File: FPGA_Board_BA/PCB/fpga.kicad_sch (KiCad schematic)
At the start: 5 parts, among them J9 Box_Header_26pin, U2 Zynq7020

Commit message: some minimal changes on the PCB on the right side
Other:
- moved on the sheet: U2B, U2C, U2D

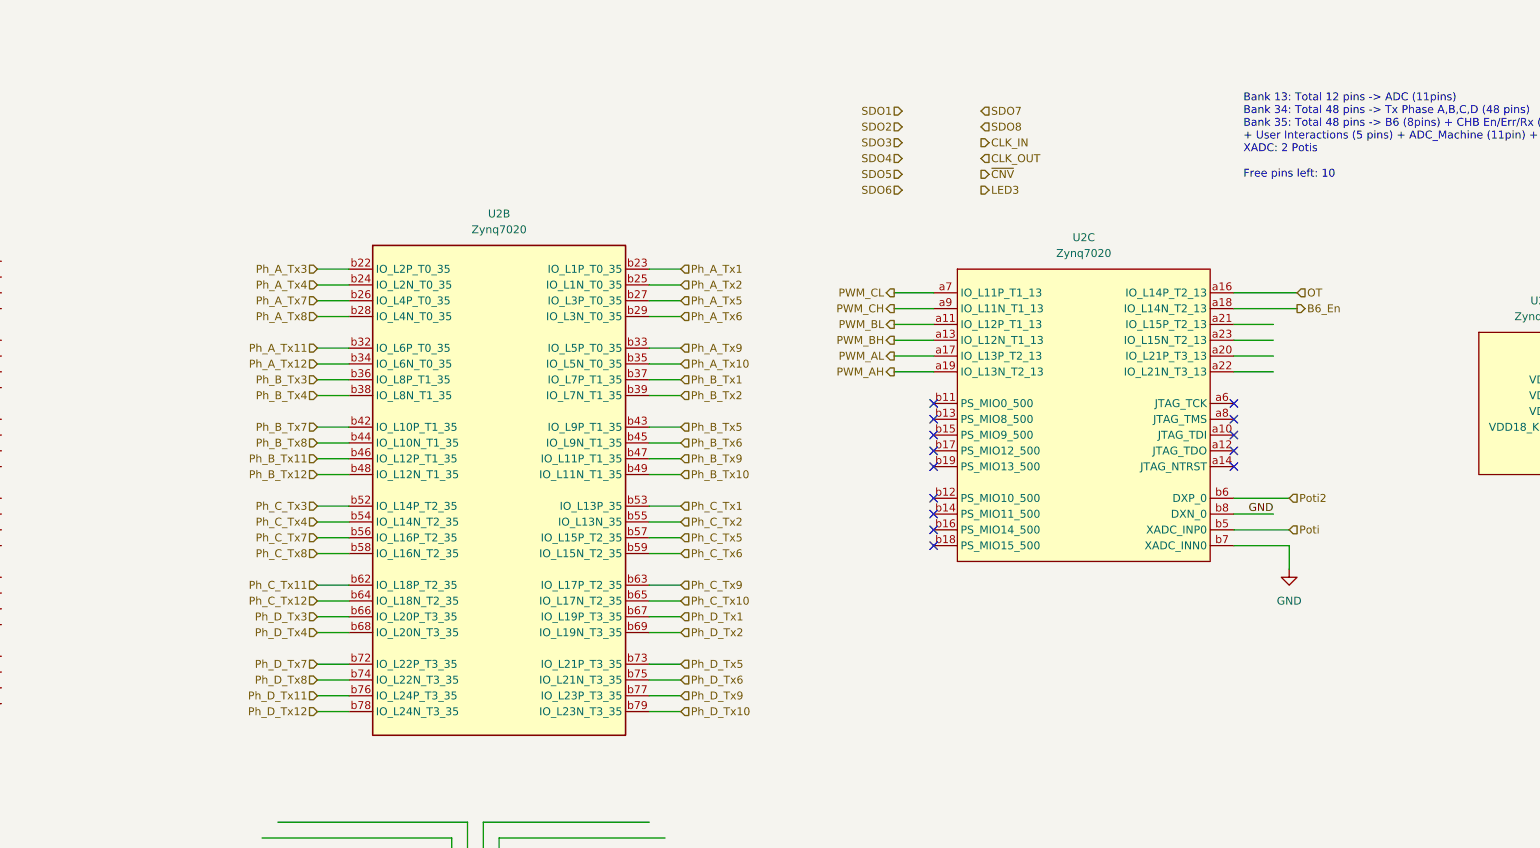
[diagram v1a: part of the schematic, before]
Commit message: added bus into schematic
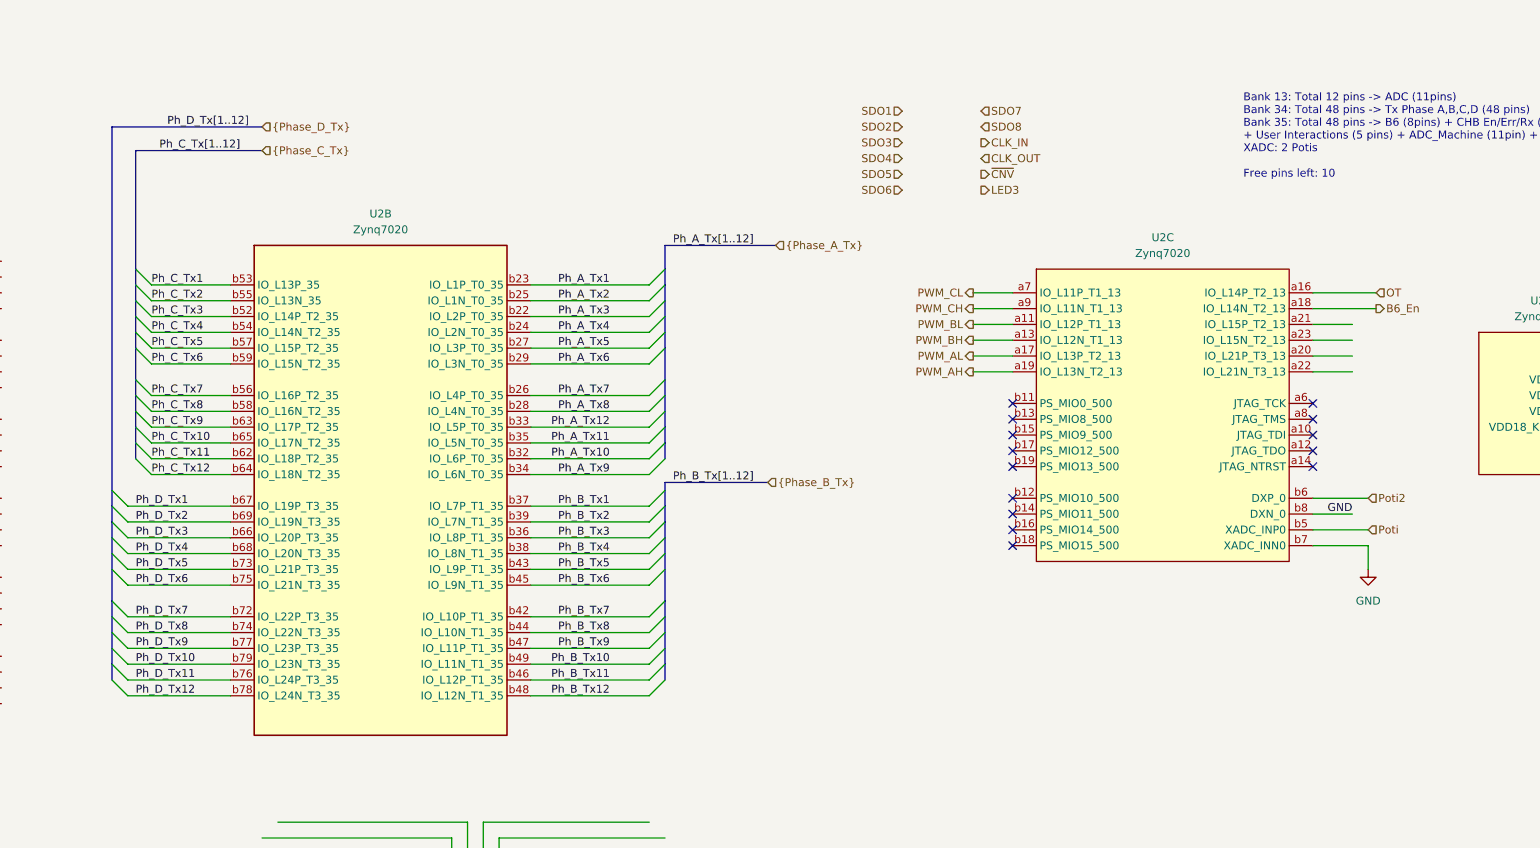
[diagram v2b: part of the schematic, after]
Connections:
- net Ph_A_Tx10: now also U2.b32 (IO_L6P_T0_35); no longer U2.b35 (IO_L5N_T0_35)
- net Ph_A_Tx11: now also U2.b35 (IO_L5N_T0_35); no longer U2.b32 (IO_L6P_T0_35)
- net Ph_A_Tx12: now also U2.b33 (IO_L5P_T0_35); no longer U2.b34 (IO_L6N_T0_35)
- net Ph_A_Tx9: now also U2.b34 (IO_L6N_T0_35); no longer U2.b33 (IO_L5P_T0_35)
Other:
- moved on the sheet: U2B, U2C

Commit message: big schematic cleanup. Added wire to bus
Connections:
- net B6_En: now also U2.a16 (IO_L14P_T2_13); no longer U2.a18 (IO_L14N_T2_13)
- net CLK_IN: now also U2.a38 (IO_L5N_T0_34)
- net CLK_OUT: now also U2.a36 (IO_L5P_T0_34)
- net OT: now also U2.a18 (IO_L14N_T2_13); no longer U2.a16 (IO_L14P_T2_13)
- net PWM_AH: now also U2.a7 (IO_L11P_T1_13); no longer U2.a19 (IO_L13N_T2_13)
- net PWM_AL: now also U2.a9 (IO_L11N_T1_13); no longer U2.a17 (IO_L13P_T2_13)
- net PWM_BH: now also U2.a11 (IO_L12P_T1_13); no longer U2.a13 (IO_L12N_T1_13)
- net PWM_BL: now also U2.a13 (IO_L12N_T1_13); no longer U2.a11 (IO_L12P_T1_13)
- net PWM_CH: now also U2.a17 (IO_L13P_T2_13); no longer U2.a9 (IO_L11N_T1_13)
- net PWM_CL: now also U2.a19 (IO_L13N_T2_13); no longer U2.a7 (IO_L11P_T1_13)
- net SDO1: now also U2.a26 (IO_L1P_T0_34)
- net SDO2: now also U2.a28 (IO_L1N_T0_34)
- net SDO3: now also U2.a27 (IO_L2P_T0_34)
- net SDO4: now also U2.a29 (IO_L2N_T0_34)
- net SDO5: now also U2.a30 (IO_L3P_T0_34)
- net SDO6: now also U2.a32 (IO_L3N_T0_34)
- net SDO7: now also U2.a31 (IO_L4P_T0_34)
- net SDO8: now also U2.a33 (IO_L4N_T0_34)
- net ~{CNV}: now also U2.a37 (IO_L6P_T0_34)
- net Err_Ph1: now reaches U2.a64 (IO_L19P_T3_34)
- net Err_Ph2: now reaches U2.a66 (IO_L19N_T3_34)
- net Err_Ph4: now reaches U2.a71 (IO_L20P_T3_34)
- net Err_Ph3: now reaches U2.a72 (IO_L20N_T3_34)
- net Rx_Ph2: now reaches U2.a73 (IO_L21N_T3_34)
- net Rx_Ph1: now reaches U2.a74 (IO_L21P_T3_34)
- net Rx_Ph3: now reaches U2.a75 (IO_L22P_T3_34)
- net En_Ph3: now reaches U2.a76 (IO_L24P_T3_34)
- net Rx_Ph4: now reaches U2.a77 (IO_L22N_T3_34)
- net En_Ph4: now reaches U2.a78 (IO_L24N_T3_34)
- net En_Ph1: now reaches U2.a79 (IO_L23P_T3_34)
- net En_Ph2: now reaches U2.a80 (IO_L23N_T3_34)
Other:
- moved on the sheet: U2A, U2B, U2C

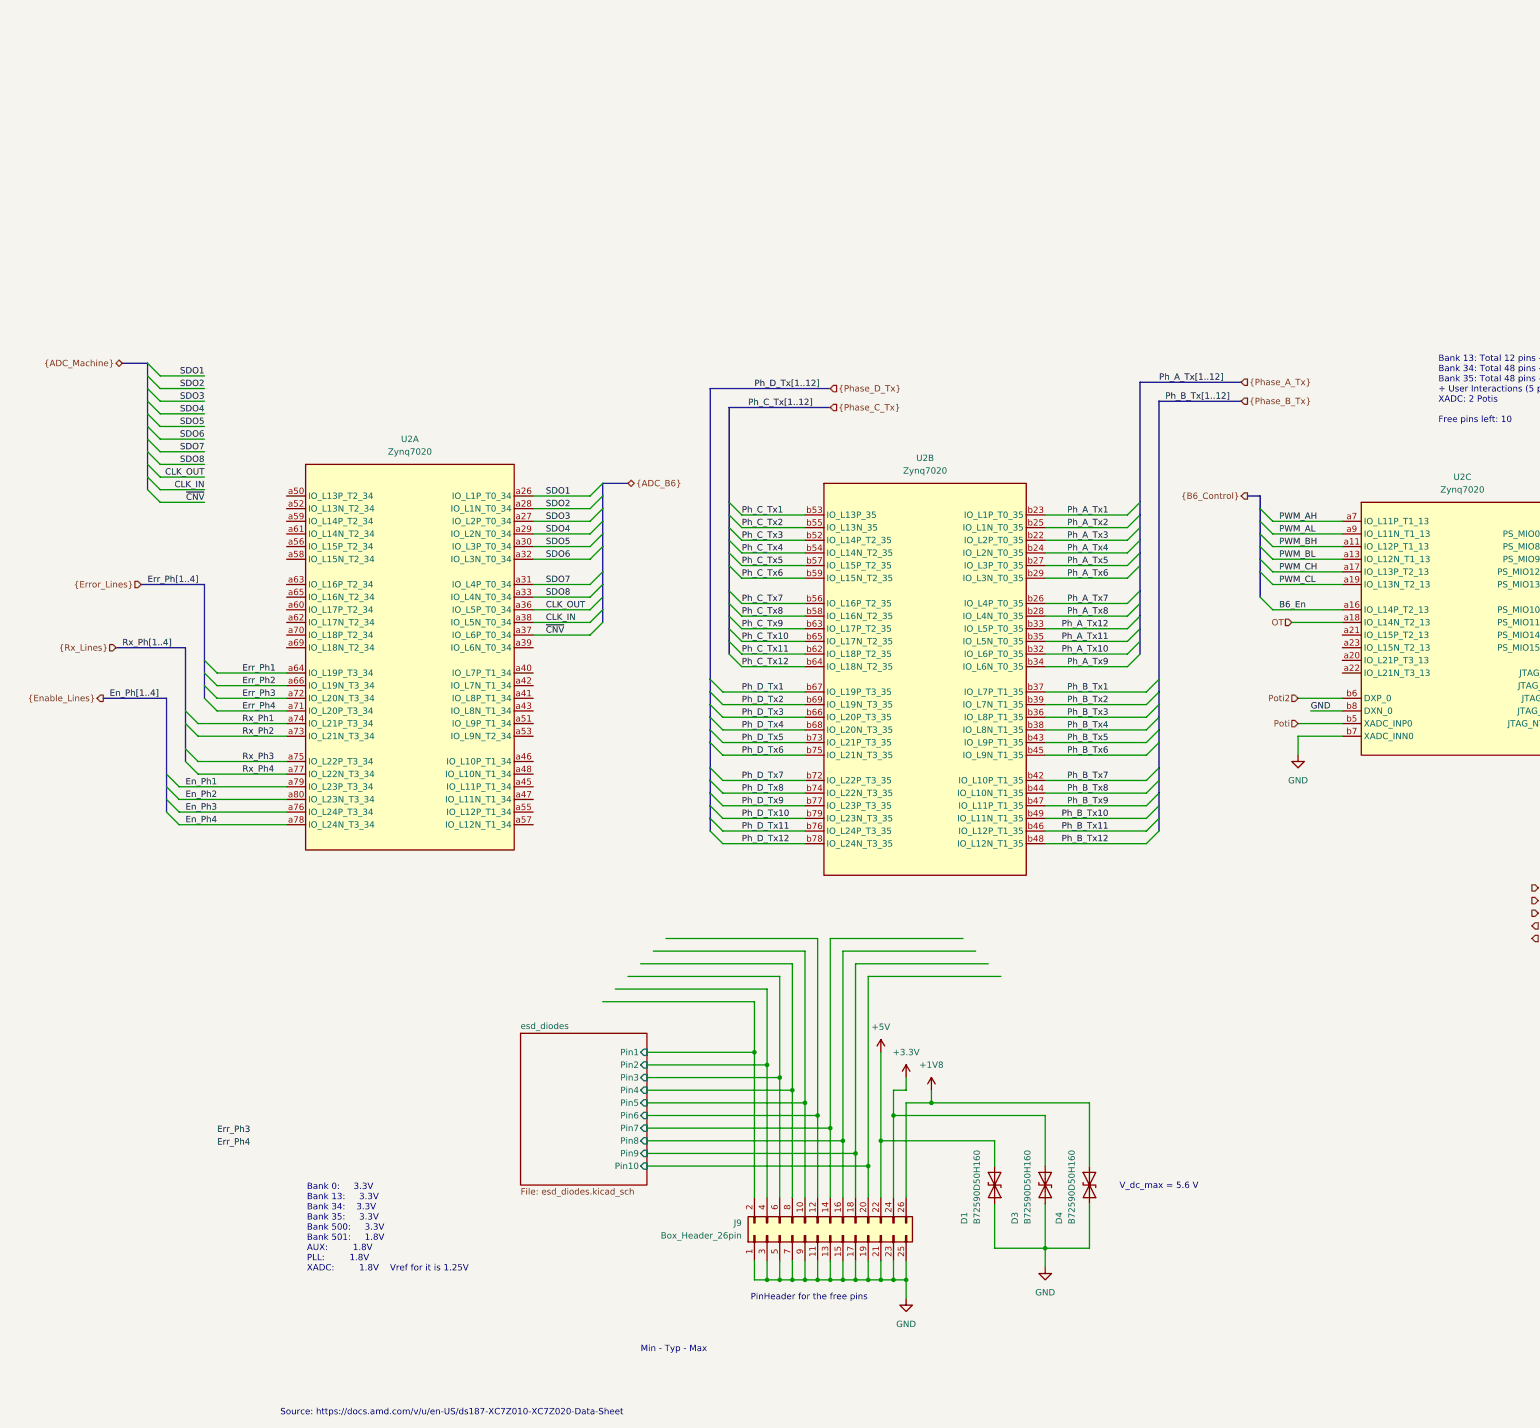
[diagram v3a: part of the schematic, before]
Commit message: PCB left side almost finished + some optimization in schematics
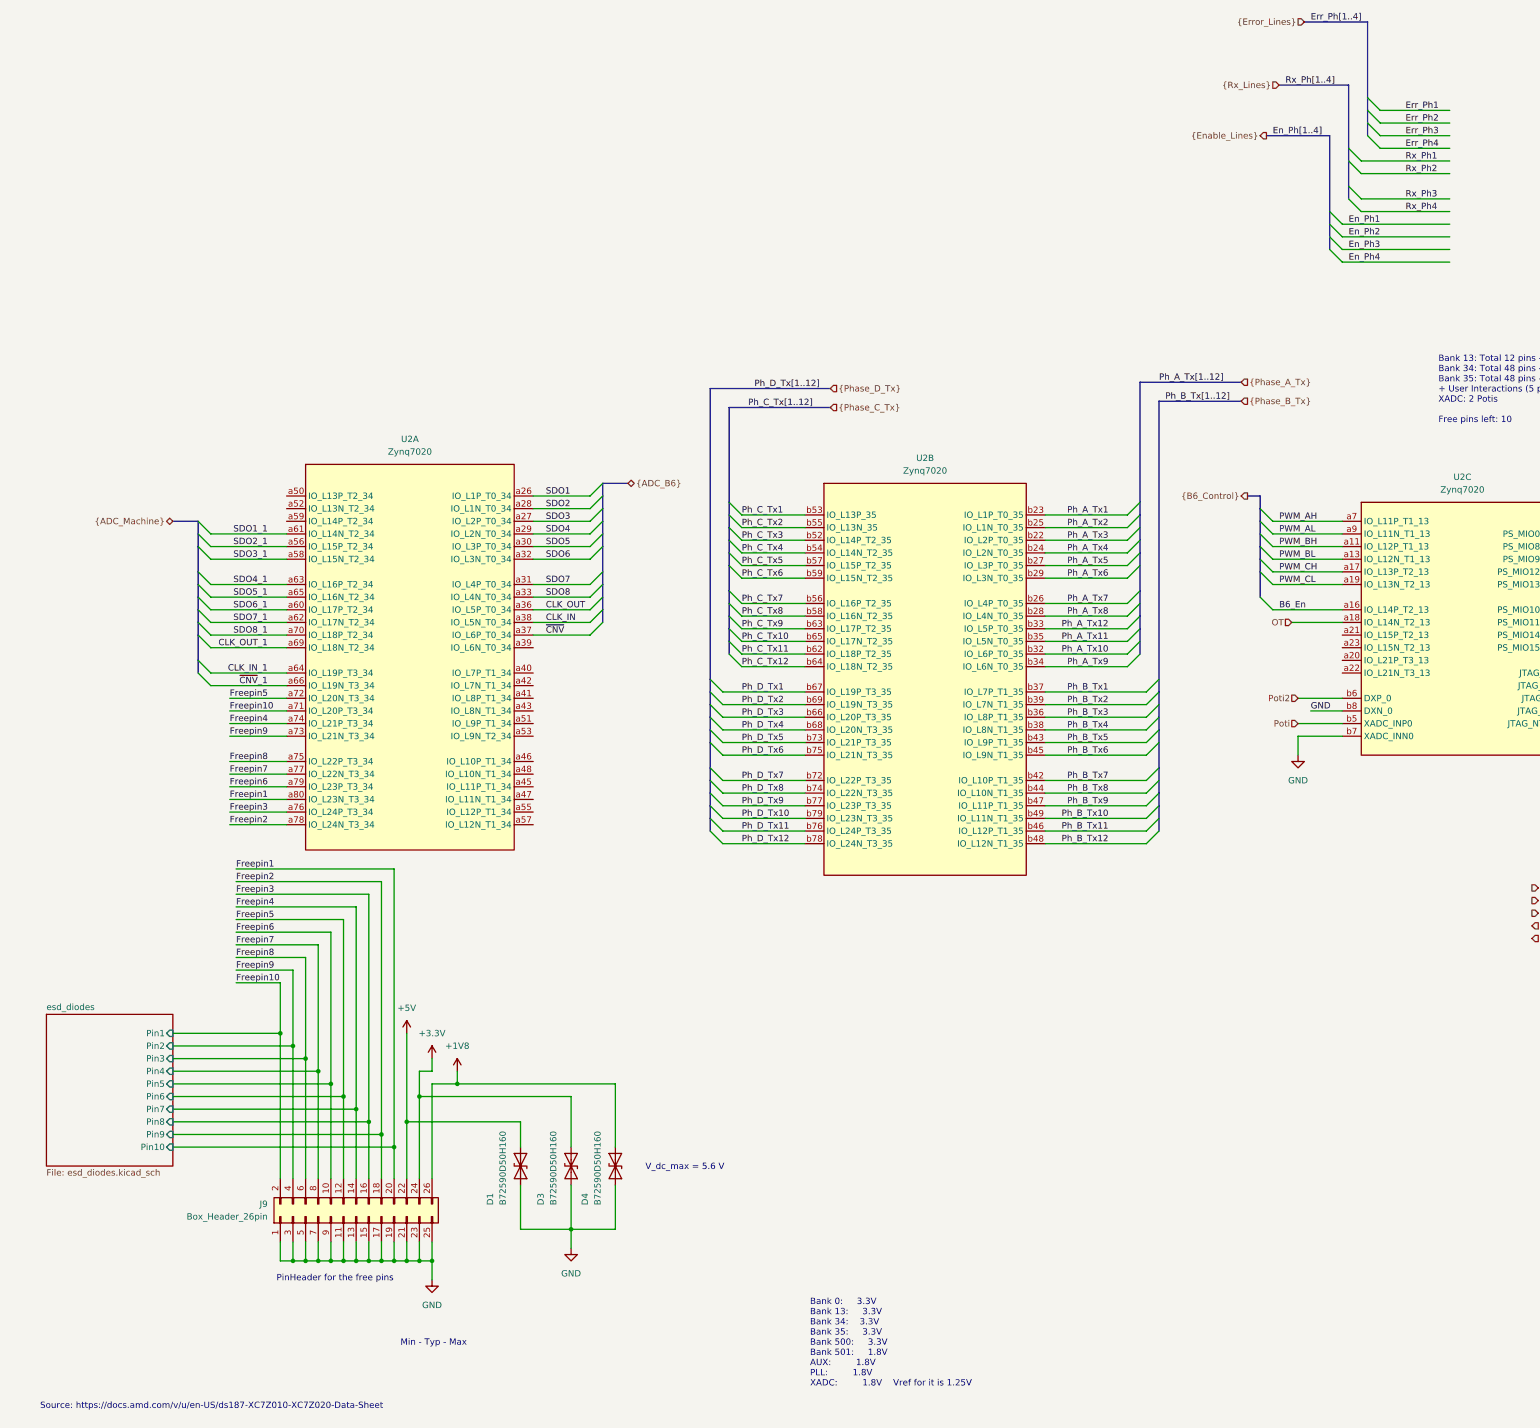
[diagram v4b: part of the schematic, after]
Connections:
- net En_Ph1: no longer U2.a79 (IO_L23P_T3_34)
- net En_Ph2: no longer U2.a80 (IO_L23N_T3_34)
- net En_Ph3: no longer U2.a76 (IO_L24P_T3_34)
- net En_Ph4: no longer U2.a78 (IO_L24N_T3_34)
- net Err_Ph1: no longer U2.a64 (IO_L19P_T3_34)
- net Err_Ph2: no longer U2.a66 (IO_L19N_T3_34)
- net Err_Ph3: no longer U2.a72 (IO_L20N_T3_34)
- net Err_Ph4: no longer U2.a71 (IO_L20P_T3_34)
- net Rx_Ph1: no longer U2.a74 (IO_L21P_T3_34)
- net Rx_Ph2: no longer U2.a73 (IO_L21N_T3_34)
- net Rx_Ph3: no longer U2.a75 (IO_L22P_T3_34)
- net Rx_Ph4: no longer U2.a77 (IO_L22N_T3_34)
- net SDO2_1: now reaches U2.a56 (IO_L15P_T2_34)
- net SDO3_1: now reaches U2.a58 (IO_L15N_T2_34)
- net SDO6_1: now reaches U2.a60 (IO_L17P_T2_34)
- net SDO1_1: now reaches U2.a61 (IO_L14N_T2_34)
- net SDO7_1: now reaches U2.a62 (IO_L17N_T2_34)
- net SDO4_1: now reaches U2.a63 (IO_L16P_T2_34)
- net SDO5_1: now reaches U2.a65 (IO_L16N_T2_34)
- net CLK_OUT_1: now reaches U2.a69 (IO_L18N_T2_34)
- net SDO8_1: now reaches U2.a70 (IO_L18P_T2_34)
- net esd_diodes/Pin1 renamed Freepin10
- net Freepin10: now also U2.a71 (IO_L20P_T3_34)
- net esd_diodes/Pin10 renamed Freepin1
- net Freepin1: now also U2.a80 (IO_L23N_T3_34)
- net esd_diodes/Pin2 renamed Freepin9
- net Freepin9: now also U2.a73 (IO_L21N_T3_34)
- net esd_diodes/Pin3 renamed Freepin8
- net Freepin8: now also U2.a75 (IO_L22P_T3_34)
- net esd_diodes/Pin4 renamed Freepin7
- net Freepin7: now also U2.a77 (IO_L22N_T3_34)
- net esd_diodes/Pin5 renamed Freepin6
- net Freepin6: now also U2.a79 (IO_L23P_T3_34)
- net esd_diodes/Pin6 renamed Freepin5
- net Freepin5: now also U2.a72 (IO_L20N_T3_34)
- net esd_diodes/Pin7 renamed Freepin4
- net Freepin4: now also U2.a74 (IO_L21P_T3_34)
- net esd_diodes/Pin8 renamed Freepin3
- net Freepin3: now also U2.a76 (IO_L24P_T3_34)
- net esd_diodes/Pin9 renamed Freepin2
- net Freepin2: now also U2.a78 (IO_L24N_T3_34)
- new net CLK_IN_1: U2.a64 (IO_L19P_T3_34)
- new net ~{CNV}_1: U2.a66 (IO_L19N_T3_34)
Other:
- moved on the sheet: D1, D3, D4, J9

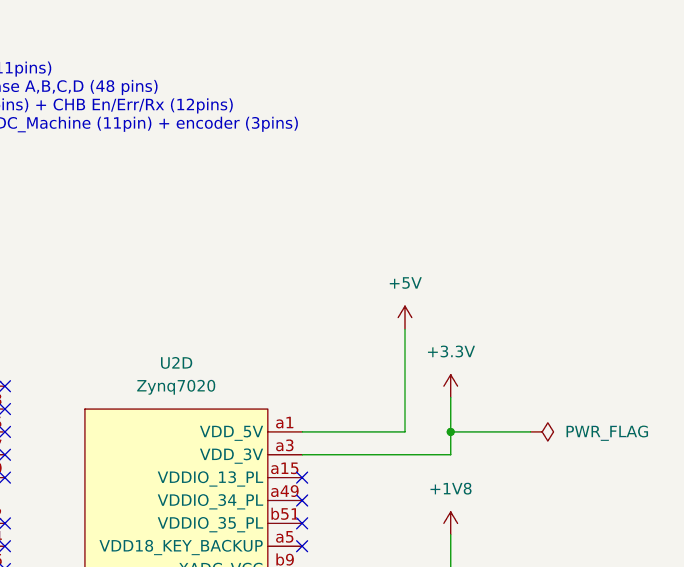
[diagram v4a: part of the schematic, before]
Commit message: layed out power supply for Zynq
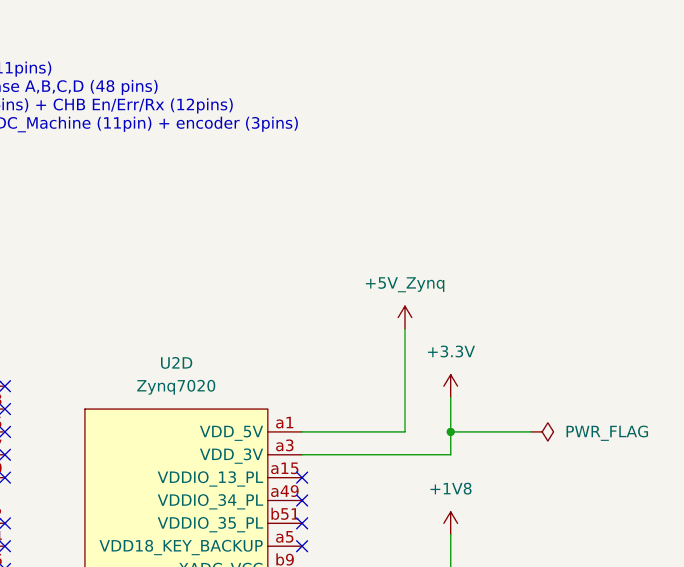
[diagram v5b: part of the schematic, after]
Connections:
- net +5V: no longer U2.a1 (VDD_5V), U2.b1 (VDD_5V)
- new net +5V_Zynq: U2.a1 (VDD_5V), U2.b1 (VDD_5V)
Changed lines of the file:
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@@
 			)
 		)
-		(property "Value" "+5V"
+		(property "Value" "+5V_Zynq"
 			(at 373.38 93.98 0)
 			(effects
